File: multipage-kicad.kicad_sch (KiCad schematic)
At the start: 0 parts

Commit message: Pages
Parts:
- added R?: R, symbol Device:R
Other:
- added sheet A (sch/a.kicad_sch)
- added sheet A1 (sch/a.kicad_sch)
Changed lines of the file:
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@@
 (kicad_sch (version 20211123) (generator eeschema)
   (paper "A4")
+  (symbol (lib_id "Device:R") (at 116.84 92.71 0) (unit 1)
+    (in_bom yes) (on_board yes) (fields_autoplaced)
+    (property "Reference" "R?" (id 0) (at 119.38 91.4399 0)
+      (effects (font (size 1.27 1.27)) (justify left))
+    )
+    (property "Value" "R" (id 1) (at 119.38 93.9799 0)
+      (effects (font (size 1.27 1.27)) (justify left))
+    )
+    (property "Footprint" "" (id 2) (at 115.062 92.71 90)
+      (effects (font (size 1.27 1.27)) hide)
+    )
+    (property "Datasheet" "~" (id 3) (at 116.84 92.71 0)
+      (effects (font (size 1.27 1.27)) hide)
+    )
+    (pin "1")
+    (pin "2")
+  )
+  (sheet (at 135.89 85.09) (size 31.75 12.7) (fields_autoplaced)
+    (stroke (width 0.1524) (type solid) (color 0 0 0 0))
+    (fill (color 0 0 0 0.0000))
+    (property "Sheet name" "A" (id 0) (at 135.89 84.3784 0)
+      (effects (font (size 1.27 1.27)) (justify left bottom))
+    )
+    (property "Sheet file" "sch/a.kicad_sch" (id 1) (at 135.89 98.3746 0)
+      (effects (font (size 1.27 1.27)) (justify left top))
+    )
+  )
+  (sheet (at 137.16 109.22) (size 31.75 12.7) (fields_autoplaced)
+    (stroke (width 0.1524) (type solid) (color 0 0 0 0))
+    (fill (color 0 0 0 0.0000))
+    (property "Sheet name" "A1" (id 0) (at 137.16 108.5084 0)
+      (effects (font (size 1.27 1.27)) (justify left bottom))
+    )
+    (property "Sheet file" "sch/a.kicad_sch" (id 1) (at 137.16 122.5046 0)
+      (effects (font (size 1.27 1.27)) (justify left top))
+    )
+  )
   (sheet_instances
     (path "/" (page "1"))
+    (path "/0999d842-9bc9-4370-bae4-7c28aeba0392" (page "2"))
+    (path "/0999d842-9bc9-4370-bae4-7c28aeba0392/af0df44c-6dac-4e54-9046-61f50d694500" (page "3"))
+    (path "/0999d842-9bc9-4370-bae4-7c28aeba0392/af0df44c-6dac-4e54-9046-61f50d694500/b8ce0eda-c484-471e-931d-2b670c8c190c" (page "4"))
+    (path "/6483d8c3-df4d-40b4-b616-c993cba432d4" (page "5"))
+    (path "/6483d8c3-df4d-40b4-b616-c993cba432d4/af0df44c-6dac-4e54-9046-61f50d694500" (page "6"))
+    (path "/6483d8c3-df4d-40b4-b616-c993cba432d4/af0df44c-6dac-4e54-9046-61f50d694500/b8ce0eda-c484-471e-931d-2b670c8c190c" (page "7"))
+    (path "/0999d842-9bc9-4370-bae4-7c28aeba0392/af0df44c-6dac-4e54-9046-61f50d694500/b8ce0eda-c484-471e-931d-2b670c8c190c/6ff9b507-1322-4901-bce9-d0ad1ae51e49" (page "8"))
+    (path "/6483d8c3-df4d-40b4-b616-c993cba432d4/af0df44c-6dac-4e54-9046-61f50d694500/b8ce0eda-c484-471e-931d-2b670c8c190c/6ff9b507-1322-4901-bce9-d0ad1ae51e49" (page "9"))
+  )
+  (symbol_instances
+    (path "/0999d842-9bc9-4370-bae4-7c28aeba0392/af0df44c-6dac-4e54-9046-61f50d694500/18014c2e-f94e-4d78-b8c5-1cf948186e55"
+      (reference "C?") (unit 1) (value "C") (footprint "")
+    )
+    (path "/6483d8c3-df4d-40b4-b616-c993cba432d4/af0df44c-6dac-4e54-9046-61f50d694500/18014c2e-f94e-4d78-b8c5-1cf948186e55"
+      (reference "C?") (unit 1) (value "C") (footprint "")
+    )
+    (path "/0999d842-9bc9-4370-bae4-7c28aeba0392/af0df44c-6dac-4e54-9046-61f50d694500/b8ce0eda-c484-471e-931d-2b670c8c190c/5f2b54e6-fe1a-426c-9428-e1edcef6cf67"
+      (reference "J?") (unit 1) (value "XLR3") (footprint "")
+    )
+    (path "/6483d8c3-df4d-40b4-b616-c993cba432d4/af0df44c-6dac-4e54-9046-61f50d694500/b8ce0eda-c484-471e-931d-2b670c8c190c/5f2b54e6-fe1a-426c-9428-e1edcef6cf67"
+      (reference "J?") (unit 1) (value "XLR3") (footprint "")
+    )
+    (path "/0999d842-9bc9-4370-bae4-7c28aeba0392/af0df44c-6dac-4e54-9046-61f50d694500/b8ce0eda-c484-471e-931d-2b670c8c190c/6ff9b507-1322-4901-bce9-d0ad1ae51e49/e5498f54-fe2f-42f0-ace5-ad56855aa87e"
+      (reference "J?") (unit 1) (value "ATX-24") (footprint "")
+    )
+    (path "/6483d8c3-df4d-40b4-b616-c993cba432d4/af0df44c-6dac-4e54-9046-61f50d694500/b8ce0eda-c484-471e-931d-2b670c8c190c/6ff9b507-1322-4901-bce9-d0ad1ae51e49/e5498f54-fe2f-42f0-ace5-ad56855aa87e"
+      (reference "J?") (unit 1) (value "ATX-24") (footprint "")
+    )
+    (path "/0999d842-9bc9-4370-bae4-7c28aeba0392/28f03c77-bdb0-420a-94cd-7aa45dcedef9"
+      (reference "L?") (unit 1) (value "L") (footprint "")
+    )
+    (path "/6483d8c3-df4d-40b4-b616-c993cba432d4/28f03c77-bdb0-420a-94cd-7aa45dcedef9"
+      (reference "L?") (unit 1) (value "L") (footprint "")
+    )
+    (path "/7d38a46f-dd8e-40d0-861b-c592f6893f0c"
+      (reference "R?") (unit 1) (value "R") (footprint "")
+    )
   )
 )

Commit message: Update
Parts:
- added R?: R, symbol Device:R
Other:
- moved on the sheet: R?
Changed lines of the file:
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@@
 (kicad_sch (version 20211123) (generator eeschema)
   (paper "A4")
-  (symbol (lib_id "Device:R") (at 116.84 92.71 0) (unit 1)
+  (symbol (lib_id "Device:R") (at 160.02 110.49 0) (mirror y) (unit 1)
     (in_bom yes) (on_board yes) (fields_autoplaced)
-    (property "Reference" "R?" (id 0) (at 119.38 91.4399 0)
+    (property "Reference" "R?" (id 0) (at 162.56 109.2199 0)
+      (effects (font (size 1.27 1.27)) (justify right))
+    )
+    (property "Value" "R" (id 1) (at 162.56 111.7599 0)
+      (effects (font (size 1.27 1.27)) (justify right))
+    )
+    (property "Footprint" "" (id 2) (at 161.798 110.49 90)
+      (effects (font (size 1.27 1.27)) hide)
+    )
+    (property "Datasheet" "~" (id 3) (at 160.02 110.49 0)
+      (effects (font (size 1.27 1.27)) hide)
+    )
+    (pin "1")
+    (pin "2")
+  )
+  (symbol (lib_id "Device:R") (at 152.4 110.49 0) (unit 1)
+    (in_bom yes) (on_board yes) (fields_autoplaced)
+    (property "Reference" "R?" (id 0) (at 154.94 109.2199 0)
       (effects (font (size 1.27 1.27)) (justify left))
     )
-    (property "Value" "R" (id 1) (at 119.38 93.9799 0)
+    (property "Value" "R" (id 1) (at 154.94 111.7599 0)
       (effects (font (size 1.27 1.27)) (justify left))
     )
-    (property "Footprint" "" (id 2) (at 115.062 92.71 90)
+    (property "Footprint" "" (id 2) (at 150.622 110.49 90)
       (effects (font (size 1.27 1.27)) hide)
     )
-    (property "Datasheet" "~" (id 3) (at 116.84 92.71 0)
+    (property "Datasheet" "~" (id 3) (at 152.4 110.49 0)
       (effects (font (size 1.27 1.27)) hide)
     )
@@
     )
   )
-  (sheet (at 137.16 109.22) (size 31.75 12.7) (fields_autoplaced)
+  (sheet (at 171.45 85.09) (size 31.75 12.7) (fields_autoplaced)
     (stroke (width 0.1524) (type solid) (color 0 0 0 0))
     (fill (color 0 0 0 0.0000))
-    (property "Sheet name" "A1" (id 0) (at 137.16 108.5084 0)
+    (property "Sheet name" "A1" (id 0) (at 171.45 84.3784 0)
       (effects (font (size 1.27 1.27)) (justify left bottom))
     )
-    (property "Sheet file" "sch/a.kicad_sch" (id 1) (at 137.16 122.5046 0)
+    (property "Sheet file" "sch/a.kicad_sch" (id 1) (at 171.45 98.3746 0)
       (effects (font (size 1.27 1.27)) (justify left top))
     )
@@
   )
   (symbol_instances
+    (path "/0999d842-9bc9-4370-bae4-7c28aeba0392/af0df44c-6dac-4e54-9046-61f50d694500/b8ce0eda-c484-471e-931d-2b670c8c190c/6ff9b507-1322-4901-bce9-d0ad1ae51e49/356074cb-e604-4934-8ff3-775e1ae5c69d"
+      (reference "#PWR?") (unit 1) (value "GND") (footprint "")
+    )
+    (path "/6483d8c3-df4d-40b4-b616-c993cba432d4/af0df44c-6dac-4e54-9046-61f50d694500/b8ce0eda-c484-471e-931d-2b670c8c190c/6ff9b507-1322-4901-bce9-d0ad1ae51e49/356074cb-e604-4934-8ff3-775e1ae5c69d"
+      (reference "#PWR?") (unit 1) (value "GND") (footprint "")
+    )
     (path "/0999d842-9bc9-4370-bae4-7c28aeba0392/af0df44c-6dac-4e54-9046-61f50d694500/18014c2e-f94e-4d78-b8c5-1cf948186e55"
       (reference "C?") (unit 1) (value "C") (footprint "")
@@
       (reference "J?") (unit 1) (value "ATX-24") (footprint "")
     )
+    (path "/0999d842-9bc9-4370-bae4-7c28aeba0392/0df6a6be-0c49-4bd6-8a7f-739372373f8f"
+      (reference "L?") (unit 1) (value "L") (footprint "")
+    )
+    (path "/6483d8c3-df4d-40b4-b616-c993cba432d4/0df6a6be-0c49-4bd6-8a7f-739372373f8f"
+      (reference "L?") (unit 1) (value "L") (footprint "")
+    )
     (path "/0999d842-9bc9-4370-bae4-7c28aeba0392/28f03c77-bdb0-420a-94cd-7aa45dcedef9"
       (reference "L?") (unit 1) (value "L") (footprint "")
@@
       (reference "L?") (unit 1) (value "L") (footprint "")
     )
+    (path "/0999d842-9bc9-4370-bae4-7c28aeba0392/75e3189a-61f1-4bd2-b13e-4b8294b03c12"
+      (reference "L?") (unit 1) (value "L") (footprint "")
+    )
+    (path "/6483d8c3-df4d-40b4-b616-c993cba432d4/75e3189a-61f1-4bd2-b13e-4b8294b03c12"
+      (reference "L?") (unit 1) (value "L") (footprint "")
+    )
+    (path "/565fed79-47a0-410d-9c77-72bb2984172c"
+      (reference "R?") (unit 1) (value "R") (footprint "")
+    )
     (path "/7d38a46f-dd8e-40d0-861b-c592f6893f0c"

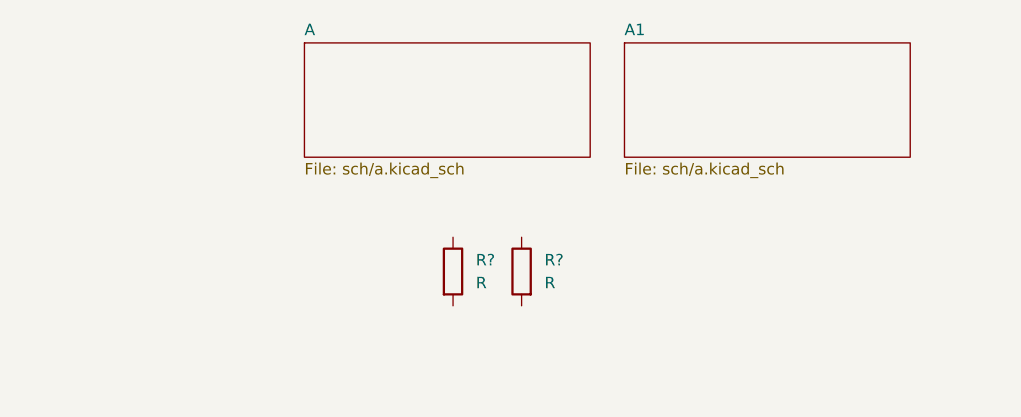
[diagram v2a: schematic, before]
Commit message: Add file and sheet instance with spaces. Anotate parts.
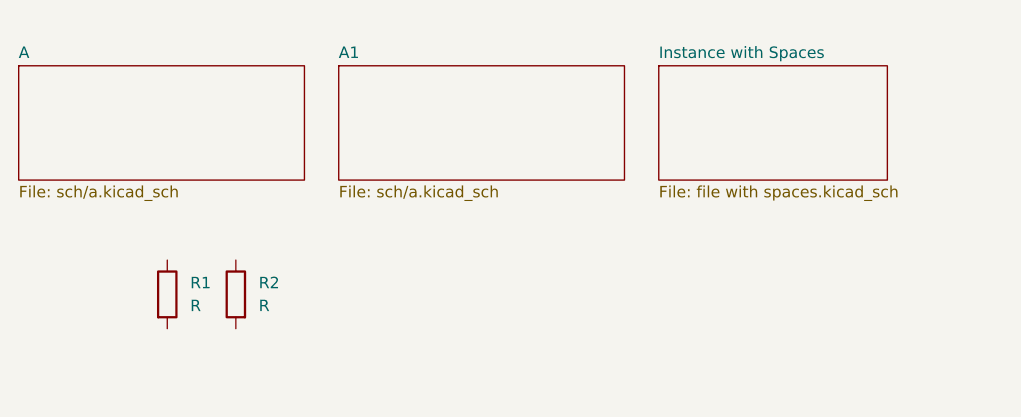
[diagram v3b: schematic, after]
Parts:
- gave numbers to parts that had none: 2
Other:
- added sheet Instance with Spaces (file with spaces.kicad_sch)
- moved on the sheet: R1, R2
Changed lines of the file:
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@@
 (kicad_sch (version 20211123) (generator eeschema)
   (paper "A4")
-  (symbol (lib_id "Device:R") (at 160.02 110.49 0) (mirror y) (unit 1)
+  (symbol (lib_id "Device:R") (at 128.27 113.03 0) (mirror y) (unit 1)
     (in_bom yes) (on_board yes) (fields_autoplaced)
-    (property "Reference" "R?" (id 0) (at 162.56 109.2199 0)
+    (property "Reference" "R2" (id 0) (at 130.81 111.7599 0)
       (effects (font (size 1.27 1.27)) (justify right))
     )
-    (property "Value" "R" (id 1) (at 162.56 111.7599 0)
+    (property "Value" "R" (id 1) (at 130.81 114.2999 0)
       (effects (font (size 1.27 1.27)) (justify right))
     )
-    (property "Footprint" "" (id 2) (at 161.798 110.49 90)
+    (property "Footprint" "" (id 2) (at 130.048 113.03 90)
       (effects (font (size 1.27 1.27)) hide)
     )
-    (property "Datasheet" "~" (id 3) (at 160.02 110.49 0)
+    (property "Datasheet" "~" (id 3) (at 128.27 113.03 0)
       (effects (font (size 1.27 1.27)) hide)
     )
@@
     (pin "2")
   )
-  (symbol (lib_id "Device:R") (at 152.4 110.49 0) (unit 1)
+  (symbol (lib_id "Device:R") (at 120.65 113.03 0) (unit 1)
     (in_bom yes) (on_board yes) (fields_autoplaced)
-    (property "Reference" "R?" (id 0) (at 154.94 109.2199 0)
+    (property "Reference" "R1" (id 0) (at 123.19 111.7599 0)
       (effects (font (size 1.27 1.27)) (justify left))
     )
-    (property "Value" "R" (id 1) (at 154.94 111.7599 0)
+    (property "Value" "R" (id 1) (at 123.19 114.2999 0)
       (effects (font (size 1.27 1.27)) (justify left))
     )
-    (property "Footprint" "" (id 2) (at 150.622 110.49 90)
+    (property "Footprint" "" (id 2) (at 118.872 113.03 90)
       (effects (font (size 1.27 1.27)) hide)
     )
-    (property "Datasheet" "~" (id 3) (at 152.4 110.49 0)
+    (property "Datasheet" "~" (id 3) (at 120.65 113.03 0)
       (effects (font (size 1.27 1.27)) hide)
     )
@@
     (pin "2")
   )
-  (sheet (at 135.89 85.09) (size 31.75 12.7) (fields_autoplaced)
+  (sheet (at 104.14 87.63) (size 31.75 12.7) (fields_autoplaced)
     (stroke (width 0.1524) (type solid) (color 0 0 0 0))
     (fill (color 0 0 0 0.0000))
-    (property "Sheet name" "A" (id 0) (at 135.89 84.3784 0)
+    (property "Sheet name" "A" (id 0) (at 104.14 86.9184 0)
       (effects (font (size 1.27 1.27)) (justify left bottom))
     )
-    (property "Sheet file" "sch/a.kicad_sch" (id 1) (at 135.89 98.3746 0)
+    (property "Sheet file" "sch/a.kicad_sch" (id 1) (at 104.14 100.9146 0)
       (effects (font (size 1.27 1.27)) (justify left top))
     )
   )
-  (sheet (at 171.45 85.09) (size 31.75 12.7) (fields_autoplaced)
+  (sheet (at 139.7 87.63) (size 31.75 12.7) (fields_autoplaced)
     (stroke (width 0.1524) (type solid) (color 0 0 0 0))
     (fill (color 0 0 0 0.0000))
-    (property "Sheet name" "A1" (id 0) (at 171.45 84.3784 0)
+    (property "Sheet name" "A1" (id 0) (at 139.7 86.9184 0)
       (effects (font (size 1.27 1.27)) (justify left bottom))
     )
-    (property "Sheet file" "sch/a.kicad_sch" (id 1) (at 171.45 98.3746 0)
+    (property "Sheet file" "sch/a.kicad_sch" (id 1) (at 139.7 100.9146 0)
+      (effects (font (size 1.27 1.27)) (justify left top))
+    )
+  )
+  (sheet (at 175.26 87.63) (size 25.4 12.7) (fields_autoplaced)
+    (stroke (width 0.1524) (type solid) (color 0 0 0 0))
+    (fill (color 0 0 0 0.0000))
+    (property "Sheet name" "Instance with Spaces" (id 0) (at 175.26 86.9184 0)
+      (effects (font (size 1.27 1.27)) (justify left bottom))
+    )
+    (property "Sheet file" "file with spaces.kicad_sch" (id 1) (at 175.26 100.9146 0)
       (effects (font (size 1.27 1.27)) (justify left top))
     )
@@
     (path "/0999d842-9bc9-4370-bae4-7c28aeba0392/af0df44c-6dac-4e54-9046-61f50d694500/b8ce0eda-c484-471e-931d-2b670c8c190c/6ff9b507-1322-4901-bce9-d0ad1ae51e49" (page "8"))
     (path "/6483d8c3-df4d-40b4-b616-c993cba432d4/af0df44c-6dac-4e54-9046-61f50d694500/b8ce0eda-c484-471e-931d-2b670c8c190c/6ff9b507-1322-4901-bce9-d0ad1ae51e49" (page "9"))
+    (path "/d6210676-7fb5-40cb-8500-7334b28a2edf" (page "10"))
   )
   (symbol_instances
     (path "/0999d842-9bc9-4370-bae4-7c28aeba0392/af0df44c-6dac-4e54-9046-61f50d694500/b8ce0eda-c484-471e-931d-2b670c8c190c/6ff9b507-1322-4901-bce9-d0ad1ae51e49/356074cb-e604-4934-8ff3-775e1ae5c69d"
-      (reference "#PWR?") (unit 1) (value "GND") (footprint "")
+      (reference "#PWR01") (unit 1) (value "GND") (footprint "")
     )
     (path "/6483d8c3-df4d-40b4-b616-c993cba432d4/af0df44c-6dac-4e54-9046-61f50d694500/b8ce0eda-c484-471e-931d-2b670c8c190c/6ff9b507-1322-4901-bce9-d0ad1ae51e49/356074cb-e604-4934-8ff3-775e1ae5c69d"
-      (reference "#PWR?") (unit 1) (value "GND") (footprint "")
+      (reference "#PWR02") (unit 1) (value "GND") (footprint "")
     )
     (path "/0999d842-9bc9-4370-bae4-7c28aeba0392/af0df44c-6dac-4e54-9046-61f50d694500/18014c2e-f94e-4d78-b8c5-1cf948186e55"
-      (reference "C?") (unit 1) (value "C") (footprint "")
+      (reference "C1") (unit 1) (value "C") (footprint "")
     )
     (path "/6483d8c3-df4d-40b4-b616-c993cba432d4/af0df44c-6dac-4e54-9046-61f50d694500/18014c2e-f94e-4d78-b8c5-1cf948186e55"
-      (reference "C?") (unit 1) (value "C") (footprint "")
+      (reference "C2") (unit 1) (value "C") (footprint "")
     )
     (path "/0999d842-9bc9-4370-bae4-7c28aeba0392/af0df44c-6dac-4e54-9046-61f50d694500/b8ce0eda-c484-471e-931d-2b670c8c190c/5f2b54e6-fe1a-426c-9428-e1edcef6cf67"
-      (reference "J?") (unit 1) (value "XLR3") (footprint "")
+      (reference "J1") (unit 1) (value "XLR3") (footprint "")
     )
     (path "/6483d8c3-df4d-40b4-b616-c993cba432d4/af0df44c-6dac-4e54-9046-61f50d694500/b8ce0eda-c484-471e-931d-2b670c8c190c/5f2b54e6-fe1a-426c-9428-e1edcef6cf67"
-      (reference "J?") (unit 1) (value "XLR3") (footprint "")
+      (reference "J2") (unit 1) (value "XLR3") (footprint "")
     )
     (path "/0999d842-9bc9-4370-bae4-7c28aeba0392/af0df44c-6dac-4e54-9046-61f50d694500/b8ce0eda-c484-471e-931d-2b670c8c190c/6ff9b507-1322-4901-bce9-d0ad1ae51e49/e5498f54-fe2f-42f0-ace5-ad56855aa87e"
-      (reference "J?") (unit 1) (value "ATX-24") (footprint "")
+      (reference "J3") (unit 1) (value "ATX-24") (footprint "")
     )
     (path "/6483d8c3-df4d-40b4-b616-c993cba432d4/af0df44c-6dac-4e54-9046-61f50d694500/b8ce0eda-c484-471e-931d-2b670c8c190c/6ff9b507-1322-4901-bce9-d0ad1ae51e49/e5498f54-fe2f-42f0-ace5-ad56855aa87e"
-      (reference "J?") (unit 1) (value "ATX-24") (footprint "")
+      (reference "J4") (unit 1) (value "ATX-24") (footprint "")
+    )
+    (path "/0999d842-9bc9-4370-bae4-7c28aeba0392/75e3189a-61f1-4bd2-b13e-4b8294b03c12"
+      (reference "L1") (unit 1) (value "L") (footprint "")
     )
     (path "/0999d842-9bc9-4370-bae4-7c28aeba0392/0df6a6be-0c49-4bd6-8a7f-739372373f8f"
-      (reference "L?") (unit 1) (value "L") (footprint "")
+      (reference "L2") (unit 1) (value "L") (footprint "")
+    )
+    (path "/0999d842-9bc9-4370-bae4-7c28aeba0392/28f03c77-bdb0-420a-94cd-7aa45dcedef9"
+      (reference "L3") (unit 1) (value "L") (footprint "")
+    )
+    (path "/6483d8c3-df4d-40b4-b616-c993cba432d4/75e3189a-61f1-4bd2-b13e-4b8294b03c12"
+      (reference "L4") (unit 1) (value "L") (footprint "")
     )
     (path "/6483d8c3-df4d-40b4-b616-c993cba432d4/0df6a6be-0c49-4bd6-8a7f-739372373f8f"
-      (reference "L?") (unit 1) (value "L") (footprint "")
-    )
-    (path "/0999d842-9bc9-4370-bae4-7c28aeba0392/28f03c77-bdb0-420a-94cd-7aa45dcedef9"
-      (reference "L?") (unit 1) (value "L") (footprint "")
+      (reference "L5") (unit 1) (value "L") (footprint "")
     )
     (path "/6483d8c3-df4d-40b4-b616-c993cba432d4/28f03c77-bdb0-420a-94cd-7aa45dcedef9"
-      (reference "L?") (unit 1) (value "L") (footprint "")
+      (reference "L6") (unit 1) (value "L") (footprint "")
     )
-    (path "/0999d842-9bc9-4370-bae4-7c28aeba0392/75e3189a-61f1-4bd2-b13e-4b8294b03c12"
-      (reference "L?") (unit 1) (value "L") (footprint "")
-    )
-    (path "/6483d8c3-df4d-40b4-b616-c993cba432d4/75e3189a-61f1-4bd2-b13e-4b8294b03c12"
-      (reference "L?") (unit 1) (value "L") (footprint "")
+    (path "/7d38a46f-dd8e-40d0-861b-c592f6893f0c"
+      (reference "R1") (unit 1) (value "R") (footprint "")
     )
     (path "/565fed79-47a0-410d-9c77-72bb2984172c"
-      (reference "R?") (unit 1) (value "R") (footprint "")
-    )
-    (path "/7d38a46f-dd8e-40d0-861b-c592f6893f0c"
-      (reference "R?") (unit 1) (value "R") (footprint "")
+      (reference "R2") (unit 1) (value "R") (footprint "")
     )
   )
